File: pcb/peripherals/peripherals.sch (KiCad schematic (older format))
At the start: 10 parts, among them J101 Conn_01x04, J102 Conn_01x04, J103 Conn_01x04, J104 Conn_01x04, J105 Conn_01x04, J106 Conn_01x04, J107 Conn_01x04, J108 Conn_01x04

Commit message: Layout finished and Gerbers generated
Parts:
- removed J101, J102, J107, J108: Conn_01x04, Socket_Strips:Socket_Strip_Straight_1x04_Pitch2.54mm, symbol Connector_Generic:Conn_01x04
- added J101, J102, J107, J108: Conn_01x05, Socket_Strips:Socket_Strip_Straight_1x05_Pitch2.54mm, symbol Connector_Generic:Conn_01x05
- added MH101, MH102, MH103, MH104: MountingHole, Mounting_Holes:MountingHole_5.3mm_M5_Pad, symbol Mechanical:MountingHole
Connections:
- net GND: now also J101.1 (Pin_1), J102.1 (Pin_1), J107.1 (Pin_1), J108.1 (Pin_1)
- net Sheet5B7230C3/EN: now also J107.5 (Pin_5)
- net Sheet5B7230C3/IN: now also J101.5 (Pin_5)
- net sheet5B6E69B5/EN: now also J107.4 (Pin_4)
- net sheet5B6E69B5/IN: now also J101.4 (Pin_4)
- net sheet5B6E69C3/EN: now also J107.3 (Pin_3)
- net sheet5B6E69C3/IN: now also J101.3 (Pin_3)
- net sheet5B6E69C4/EN: now also J107.2 (Pin_2)
- net sheet5B6E69C4/IN: now also J101.2 (Pin_2)
- net sheet5B6E6A5A/EN: now also J108.5 (Pin_5)
- net sheet5B6E6A5A/IN: now also J102.5 (Pin_5)
- net sheet5B6E6A5B/EN: now also J108.4 (Pin_4)
- net sheet5B6E6A5B/IN: now also J102.4 (Pin_4)
- net sheet5B6E6A5C/EN: now also J108.3 (Pin_3)
- net sheet5B6E6A5C/IN: now also J102.3 (Pin_3)
- net sheet5B6E6A5D/EN: now also J108.2 (Pin_2)
- net sheet5B6E6A5D/IN: now also J102.2 (Pin_2)
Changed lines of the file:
@@
 Wire Wire Line
 	950  2850 1100 2850
-$Comp
-L Connector_Generic:Conn_01x04 J101
-U 1 1 5B6FBC4E
+Wire Wire Line
+	3400 3950 3900 3950
+Wire Wire Line
+	3900 3950 3900 4250
+Wire Wire Line
+	3900 4250 4050 4250
+Wire Wire Line
+	3400 3850 3900 3850
+Wire Wire Line
+	3900 3850 3900 3550
+Wire Wire Line
+	3900 3550 4050 3550
+Wire Wire Line
+	3400 3750 3850 3750
+Wire Wire Line
+	3850 3750 3850 2800
+Wire Wire Line
+	3850 2800 4050 2800
+Wire Wire Line
+	3400 3650 3800 3650
+Wire Wire Line
+	3800 3650 3800 2100
+Wire Wire Line
+	3800 2100 4050 2100
+Wire Wire Line
+	3400 2300 3600 2300
+Wire Wire Line
+	3600 2300 3600 2600
+Wire Wire Line
+	3600 2600 4050 2600
+Wire Wire Line
+	3400 2400 3550 2400
+Wire Wire Line
+	3550 2400 3550 3350
+Wire Wire Line
+	3550 3350 4050 3350
+Wire Wire Line
+	3400 2500 3500 2500
+Wire Wire Line
+	3500 2500 3500 4050
+Wire Wire Line
+	3500 4050 4050 4050
+Wire Wire Line
+	3400 2200 3600 2200
+Wire Wire Line
+	3600 2200 3600 1900
+Wire Wire Line
+	3600 1900 4050 1900
+Wire Wire Line
+	6750 3950 7250 3950
+Wire Wire Line
+	7250 3950 7250 4250
+Wire Wire Line
+	7250 4250 7400 4250
+Wire Wire Line
+	6750 3850 7250 3850
+Wire Wire Line
+	7250 3850 7250 3550
+Wire Wire Line
+	7250 3550 7400 3550
+Wire Wire Line
+	6750 3750 7200 3750
+Wire Wire Line
+	7200 3750 7200 2800
+Wire Wire Line
+	7200 2800 7400 2800
+Wire Wire Line
+	6750 3650 7150 3650
+Wire Wire Line
+	7150 3650 7150 2100
+Wire Wire Line
+	7150 2100 7400 2100
+Wire Wire Line
+	6750 2300 6950 2300
+Wire Wire Line
+	6950 2300 6950 2600
+Wire Wire Line
+	6950 2600 7400 2600
+Wire Wire Line
+	6750 2400 6900 2400
+Wire Wire Line
+	6900 2400 6900 3350
+Wire Wire Line
+	6900 3350 7400 3350
+Wire Wire Line
+	6750 2500 6850 2500
+Wire Wire Line
+	6850 2500 6850 4050
+Wire Wire Line
+	6850 4050 7400 4050
+Wire Wire Line
+	6750 2200 6950 2200
+Wire Wire Line
+	6950 2200 6950 1900
+Wire Wire Line
+	6950 1900 7400 1900
+$Comp
+L Connector_Generic:Conn_01x05 J101
+U 1 1 5B71A22D
 P 3200 2400
 F 0 "J101" H 3120 1975 50  0000 C CNN
-F 1 "Conn_01x04" H 3120 2066 50  0000 C CNN
-F 2 "Socket_Strips:Socket_Strip_Straight_1x04_Pitch2.54mm" H 3200 2400 50  0001 C CNN
+F 1 "Conn_01x05" H 3120 2066 50  0000 C CNN
+F 2 "Socket_Strips:Socket_Strip_Straight_1x05_Pitch2.54mm" H 3200 2400 50  0001 C CNN
 F 3 "~" H 3200 2400 50  0001 C CNN
 F 4 "NoPart" H 3200 2400 50  0001 C CNN "Mouser"
@@
 $EndComp
 $Comp
-L Connector_Generic:Conn_01x04 J107
-U 1 1 5B6FBCEC
+L power:GND #PWR0105
+U 1 1 5B71A5D7
+P 3450 2700
+F 0 "#PWR0105" H 3450 2450 50  0001 C CNN
+F 1 "GND" H 3455 2527 50  0000 C CNN
+F 2 "" H 3450 2700 50  0001 C CNN
+F 3 "" H 3450 2700 50  0001 C CNN
+	1    3450 2700
+	1    0    0    -1
+$EndComp
+Wire Wire Line
+	3450 2700 3450 2600
+Wire Wire Line
+	3450 2600 3400 2600
+$Comp
+L Connector_Generic:Conn_01x05 J107
+U 1 1 5B71D263
 P 3200 3850
 F 0 "J107" H 3120 3425 50  0000 C CNN
-F 1 "Conn_01x04" H 3120 3516 50  0000 C CNN
-F 2 "Socket_Strips:Socket_Strip_Straight_1x04_Pitch2.54mm" H 3200 3850 50  0001 C CNN
+F 1 "Conn_01x05" H 3120 3516 50  0000 C CNN
+F 2 "Socket_Strips:Socket_Strip_Straight_1x05_Pitch2.54mm" H 3200 3850 50  0001 C CNN
 F 3 "~" H 3200 3850 50  0001 C CNN
 F 4 "NoPart" H 3200 3850 50  0001 C CNN "Mouser"
@@
 	-1   0    0    1
 $EndComp
-Wire Wire Line
-	3400 3950 3900 3950
-Wire Wire Line
-	3900 3950 3900 4250
-Wire Wire Line
-	3900 4250 4050 4250
-Wire Wire Line
-	3400 3850 3900 3850
-Wire Wire Line
-	3900 3850 3900 3550
-Wire Wire Line
-	3900 3550 4050 3550
-Wire Wire Line
-	3400 3750 3850 3750
-Wire Wire Line
-	3850 3750 3850 2800
-Wire Wire Line
-	3850 2800 4050 2800
-Wire Wire Line
-	3400 3650 3800 3650
-Wire Wire Line
-	3800 3650 3800 2100
-Wire Wire Line
-	3800 2100 4050 2100
-Wire Wire Line
-	3400 2300 3600 2300
-Wire Wire Line
-	3600 2300 3600 2600
-Wire Wire Line
-	3600 2600 4050 2600
-Wire Wire Line
-	3400 2400 3550 2400
-Wire Wire Line
-	3550 2400 3550 3350
-Wire Wire Line
-	3550 3350 4050 3350
-Wire Wire Line
-	3400 2500 3500 2500
-Wire Wire Line
-	3500 2500 3500 4050
-Wire Wire Line
-	3500 4050 4050 4050
-Wire Wire Line
-	3400 2200 3600 2200
-Wire Wire Line
-	3600 2200 3600 1900
-Wire Wire Line
-	3600 1900 4050 1900
-$Comp
-L Connector_Generic:Conn_01x04 J102
-U 1 1 5B70643C
+$Comp
+L Connector_Generic:Conn_01x05 J102
+U 1 1 5B71D2AF
 P 6550 2400
 F 0 "J102" H 6470 1975 50  0000 C CNN
-F 1 "Conn_01x04" H 6470 2066 50  0000 C CNN
-F 2 "Socket_Strips:Socket_Strip_Straight_1x04_Pitch2.54mm" H 6550 2400 50  0001 C CNN
+F 1 "Conn_01x05" H 6470 2066 50  0000 C CNN
+F 2 "Socket_Strips:Socket_Strip_Straight_1x05_Pitch2.54mm" H 6550 2400 50  0001 C CNN
 F 3 "~" H 6550 2400 50  0001 C CNN
 F 4 "NoPart" H 6550 2400 50  0001 C CNN "Mouser"
@@
 $EndComp
 $Comp
-L Connector_Generic:Conn_01x04 J108
-U 1 1 5B706443
+L Connector_Generic:Conn_01x05 J108
+U 1 1 5B71D307
 P 6550 3850
 F 0 "J108" H 6470 3425 50  0000 C CNN
-F 1 "Conn_01x04" H 6470 3516 50  0000 C CNN
-F 2 "Socket_Strips:Socket_Strip_Straight_1x04_Pitch2.54mm" H 6550 3850 50  0001 C CNN
+F 1 "Conn_01x05" H 6470 3516 50  0000 C CNN
+F 2 "Socket_Strips:Socket_Strip_Straight_1x05_Pitch2.54mm" H 6550 3850 50  0001 C CNN
 F 3 "~" H 6550 3850 50  0001 C CNN
 F 4 "NoPart" H 6550 3850 50  0001 C CNN "Mouser"
@@
 	-1   0    0    1
 $EndComp
-Wire Wire Line
-	6750 3950 7250 3950
-Wire Wire Line
-	7250 3950 7250 4250
-Wire Wire Line
-	7250 4250 7400 4250
-Wire Wire Line
-	6750 3850 7250 3850
-Wire Wire Line
-	7250 3850 7250 3550
-Wire Wire Line
-	7250 3550 7400 3550
-Wire Wire Line
-	6750 3750 7200 3750
-Wire Wire Line
-	7200 3750 7200 2800
-Wire Wire Line
-	7200 2800 7400 2800
-Wire Wire Line
-	6750 3650 7150 3650
-Wire Wire Line
-	7150 3650 7150 2100
-Wire Wire Line
-	7150 2100 7400 2100
-Wire Wire Line
-	6750 2300 6950 2300
-Wire Wire Line
-	6950 2300 6950 2600
-Wire Wire Line
-	6950 2600 7400 2600
-Wire Wire Line
-	6750 2400 6900 2400
-Wire Wire Line
-	6900 2400 6900 3350
-Wire Wire Line
-	6900 3350 7400 3350
-Wire Wire Line
-	6750 2500 6850 2500
-Wire Wire Line
-	6850 2500 6850 4050
-Wire Wire Line
-	6850 4050 7400 4050
-Wire Wire Line
-	6750 2200 6950 2200
-Wire Wire Line
-	6950 2200 6950 1900
-Wire Wire Line
-	6950 1900 7400 1900
+$Comp
+L power:GND #PWR0107
+U 1 1 5B71D394
+P 3450 4200
+F 0 "#PWR0107" H 3450 3950 50  0001 C CNN
+F 1 "GND" H 3455 4027 50  0000 C CNN
+F 2 "" H 3450 4200 50  0001 C CNN
+F 3 "" H 3450 4200 50  0001 C CNN
+	1    3450 4200
+	1    0    0    -1
+$EndComp
+Wire Wire Line
+	3450 4200 3450 4050
+Wire Wire Line
+	3450 4050 3400 4050
+$Comp
+L power:GND #PWR0108
+U 1 1 5B720152
+P 6800 4200
+F 0 "#PWR0108" H 6800 3950 50  0001 C CNN
+F 1 "GND" H 6805 4027 50  0000 C CNN
+F 2 "" H 6800 4200 50  0001 C CNN
+F 3 "" H 6800 4200 50  0001 C CNN
+	1    6800 4200
+	1    0    0    -1
+$EndComp
+Wire Wire Line
+	6800 4200 6800 4050
+Wire Wire Line
+	6800 4050 6750 4050
+$Comp
+L power:GND #PWR0106
+U 1 1 5B723175
+P 6800 2750
+F 0 "#PWR0106" H 6800 2500 50  0001 C CNN
+F 1 "GND" H 6805 2577 50  0000 C CNN
+F 2 "" H 6800 2750 50  0001 C CNN
+F 3 "" H 6800 2750 50  0001 C CNN
+	1    6800 2750
+	1    0    0    -1
+$EndComp
+Wire Wire Line
+	6800 2750 6800 2600
+Wire Wire Line
+	6800 2600 6750 2600
+$Comp
+L Mechanical:MountingHole MH101
+U 1 1 5B72BC06
+P 2300 6000
+F 0 "MH101" H 2400 6046 50  0000 L CNN
+F 1 "MountingHole" H 2400 5955 50  0000 L CNN
+F 2 "Mounting_Holes:MountingHole_5.3mm_M5_Pad" H 2300 6000 50  0001 C CNN
+F 3 "~" H 2300 6000 50  0001 C CNN
+F 4 "NoPart" H 2300 6000 50  0001 C CNN "Mouser"
+	1    2300 6000
+	1    0    0    -1
+$EndComp
+$Comp
+L Mechanical:MountingHole MH102
+U 1 1 5B731ED4
+P 2300 6250
+F 0 "MH102" H 2400 6296 50  0000 L CNN
+F 1 "MountingHole" H 2400 6205 50  0000 L CNN
+F 2 "Mounting_Holes:MountingHole_5.3mm_M5_Pad" H 2300 6250 50  0001 C CNN
+F 3 "~" H 2300 6250 50  0001 C CNN
+F 4 "NoPart" H 2300 6250 50  0001 C CNN "Mouser"
+	1    2300 6250
+	1    0    0    -1
+$EndComp
+$Comp
+L Mechanical:MountingHole MH103
+U 1 1 5B734FC8
+P 2300 6550
+F 0 "MH103" H 2400 6596 50  0000 L CNN
+F 1 "MountingHole" H 2400 6505 50  0000 L CNN
+F 2 "Mounting_Holes:MountingHole_5.3mm_M5_Pad" H 2300 6550 50  0001 C CNN
+F 3 "~" H 2300 6550 50  0001 C CNN
+F 4 "NoPart" H 2300 6550 50  0001 C CNN "Mouser"
+	1    2300 6550
+	1    0    0    -1
+$EndComp
+$Comp
+L Mechanical:MountingHole MH104
+U 1 1 5B734FCF
+P 2300 6800
+F 0 "MH104" H 2400 6846 50  0000 L CNN
+F 1 "MountingHole" H 2400 6755 50  0000 L CNN
+F 2 "Mounting_Holes:MountingHole_5.3mm_M5_Pad" H 2300 6800 50  0001 C CNN
+F 3 "~" H 2300 6800 50  0001 C CNN
+F 4 "NoPart" H 2300 6800 50  0001 C CNN "Mouser"
+	1    2300 6800
+	1    0    0    -1
+$EndComp
 $EndSCHEMATC

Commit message: Save before autotile
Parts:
- added C101, C102: 470uF, Capacitors_ThroughHole:CP_Radial_D10.0mm_P5.00mm, symbol Device:C_Small
- added C103, C104: 1000uF, Capacitors_ThroughHole:CP_Radial_D18.0mm_P7.50mm, symbol Device:C_Small
- J103, J104, J105, J106: footprint peripherals:Conn-4-8mmx6mm -> peripherals:Conn-4-8mmx3mm
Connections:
- net +BATT: now also C101.1, C102.1, C103.1, C104.1
- net GND: now also C101.2, C102.2, C103.2, C104.2
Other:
- moved on the sheet: J101, J102, J103, J104, J105, J106, J107, J108

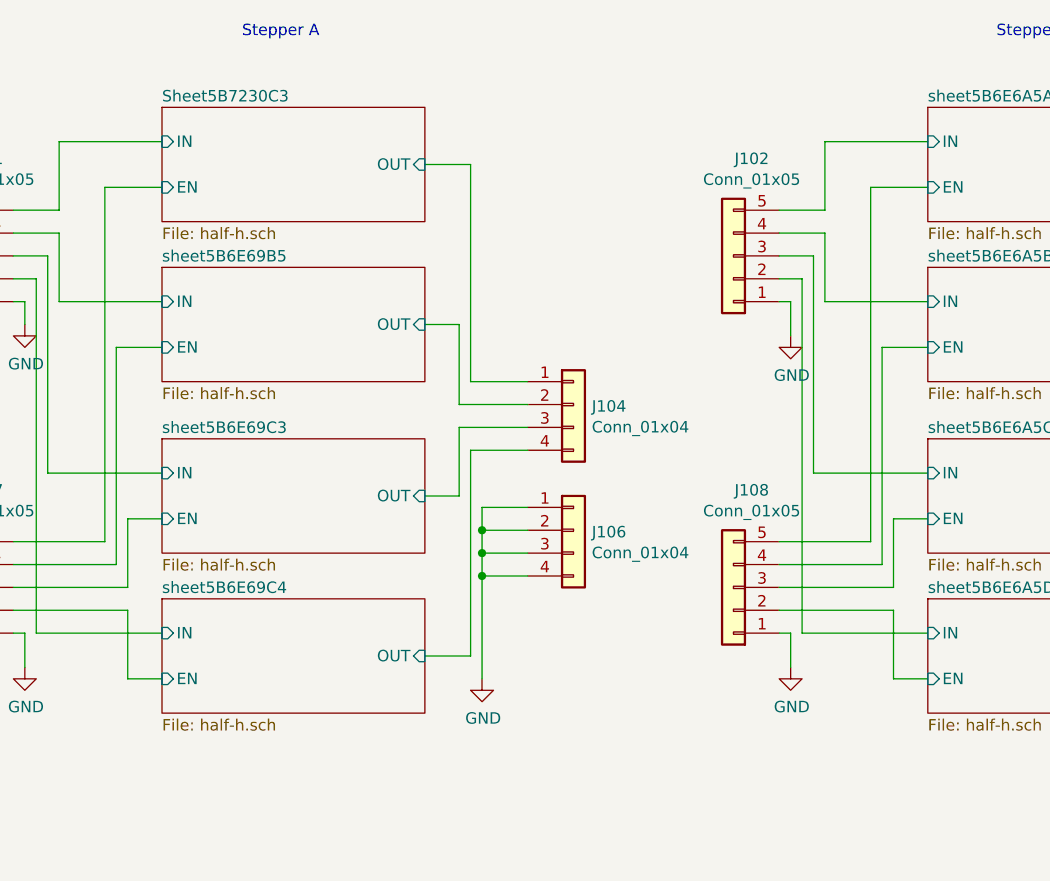
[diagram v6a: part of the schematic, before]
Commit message: Redesign peripheral PCB, simulate photodiode circuit
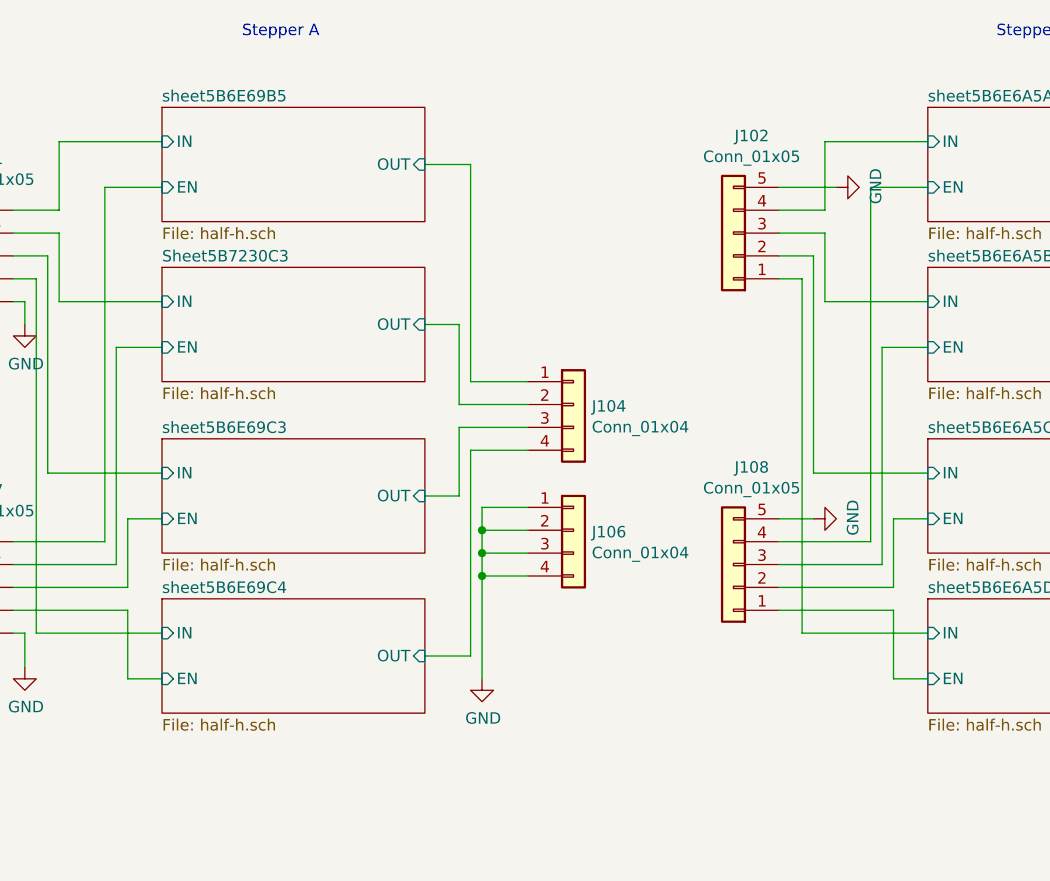
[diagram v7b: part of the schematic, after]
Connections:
- net GND: now also J102.5 (Pin_5), J108.5 (Pin_5); no longer J102.1 (Pin_1), J108.1 (Pin_1)
- net Sheet5B7230C3/EN: now also J107.4 (Pin_4); no longer J107.5 (Pin_5)
- net Sheet5B7230C3/IN: now also J101.4 (Pin_4); no longer J101.5 (Pin_5)
- net Sheet5B7230C3/OUT: now also J104.2 (Pin_2); no longer J104.1 (Pin_1)
- net sheet5B6E69B5/EN: now also J107.5 (Pin_5); no longer J107.4 (Pin_4)
- net sheet5B6E69B5/IN: now also J101.5 (Pin_5); no longer J101.4 (Pin_4)
- net sheet5B6E69B5/OUT: now also J104.1 (Pin_1); no longer J104.2 (Pin_2)
- net sheet5B6E6A5A/EN: now also J108.4 (Pin_4); no longer J108.5 (Pin_5)
- net sheet5B6E6A5A/IN: now also J102.4 (Pin_4); no longer J102.5 (Pin_5)
- net sheet5B6E6A5B/EN: now also J108.3 (Pin_3); no longer J108.4 (Pin_4)
- net sheet5B6E6A5B/IN: now also J102.3 (Pin_3); no longer J102.4 (Pin_4)
- net sheet5B6E6A5C/EN: now also J108.2 (Pin_2); no longer J108.3 (Pin_3)
- net sheet5B6E6A5C/IN: now also J102.2 (Pin_2); no longer J102.3 (Pin_3)
- net sheet5B6E6A5D/EN: now also J108.1 (Pin_1); no longer J108.2 (Pin_2)
- net sheet5B6E6A5D/IN: now also J102.1 (Pin_1); no longer J102.2 (Pin_2)
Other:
- moved on the sheet: J102, J108
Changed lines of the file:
@@
 $EndDescr
 $Sheet
-S 4850 1750 1150 500
+S 4850 2450 1150 500
 U 5B7230C4
 F0 "Sheet5B7230C3" 50
+F1 "half-h.sch" 50
+F2 "OUT" I R 6000 2700 50
+F3 "IN" I L 4850 2600 50
+F4 "EN" I L 4850 2800 50
+$EndSheet
+$Sheet
+S 4850 1750 1150 500
+U 5B6E69BA
+F0 "sheet5B6E69B5" 50
 F1 "half-h.sch" 50
 F2 "OUT" I R 6000 2000 50
 F3 "IN" I L 4850 1900 50
 F4 "EN" I L 4850 2100 50
-$EndSheet
-$Sheet
-S 4850 2450 1150 500
-U 5B6E69BA
-F0 "sheet5B6E69B5" 50
-F1 "half-h.sch" 50
-F2 "OUT" I R 6000 2700 50
-F3 "IN" I L 4850 2600 50
-F4 "EN" I L 4850 2800 50
 $EndSheet
 $Sheet
@@
 	7700 2400 7700 3350
 Wire Wire Line
-	7700 3350 8200 3350
-Wire Wire Line
 	7550 2500 7650 2500
 Wire Wire Line
@@
 L Connector_Generic:Conn_01x05 J102
 U 1 1 5B71D2AF
-P 7350 2400
-F 0 "J102" H 7270 1975 50  0000 C CNN
-F 1 "Conn_01x05" H 7270 2066 50  0000 C CNN
-F 2 "Socket_Strips:Socket_Strip_Straight_1x05_Pitch2.54mm" H 7350 2400 50  0001 C CNN
-F 3 "~" H 7350 2400 50  0001 C CNN
-F 4 "NoPart" H 7350 2400 50  0001 C CNN "Mouser"
-	1    7350 2400
+P 7350 2300
+F 0 "J102" H 7270 1875 50  0000 C CNN
+F 1 "Conn_01x05" H 7270 1966 50  0000 C CNN
+F 2 "Socket_Strips:Socket_Strip_Straight_1x05_Pitch2.54mm" H 7350 2300 50  0001 C CNN
+F 3 "~" H 7350 2300 50  0001 C CNN
+F 4 "NoPart" H 7350 2300 50  0001 C CNN "Mouser"
+	1    7350 2300
 	-1   0    0    1
 $EndComp
@@
 L Connector_Generic:Conn_01x05 J108
 U 1 1 5B71D307
-P 7350 3850
-F 0 "J108" H 7270 3425 50  0000 C CNN
-F 1 "Conn_01x05" H 7270 3516 50  0000 C CNN
-F 2 "Socket_Strips:Socket_Strip_Straight_1x05_Pitch2.54mm" H 7350 3850 50  0001 C CNN
-F 3 "~" H 7350 3850 50  0001 C CNN
-F 4 "NoPart" H 7350 3850 50  0001 C CNN "Mouser"
-	1    7350 3850
+P 7350 3750
+F 0 "J108" H 7270 3325 50  0000 C CNN
+F 1 "Conn_01x05" H 7270 3416 50  0000 C CNN
+F 2 "Socket_Strips:Socket_Strip_Straight_1x05_Pitch2.54mm" H 7350 3750 50  0001 C CNN
+F 3 "~" H 7350 3750 50  0001 C CNN
+F 4 "NoPart" H 7350 3750 50  0001 C CNN "Mouser"
+	1    7350 3750
 	-1   0    0    1
 $EndComp
@@
 L power:GND #PWR0108
 U 1 1 5B720152
-P 7600 4200
-F 0 "#PWR0108" H 7600 3950 50  0001 C CNN
-F 1 "GND" H 7605 4027 50  0000 C CNN
-F 2 "" H 7600 4200 50  0001 C CNN
-F 3 "" H 7600 4200 50  0001 C CNN
-	1    7600 4200
-	1    0    0    -1
-$EndComp
-Wire Wire Line
-	7600 4200 7600 4050
-Wire Wire Line
-	7600 4050 7550 4050
+P 7700 3550
+F 0 "#PWR0108" H 7700 3300 50  0001 C CNN
+F 1 "GND" H 7705 3377 50  0000 C CNN
+F 2 "" H 7700 3550 50  0001 C CNN
+F 3 "" H 7700 3550 50  0001 C CNN
+	1    7700 3550
+	0    -1   -1   0
+$EndComp
 $Comp
 L power:GND #PWR0106
 U 1 1 5B723175
-P 7600 2750
-F 0 "#PWR0106" H 7600 2500 50  0001 C CNN
-F 1 "GND" H 7605 2577 50  0000 C CNN
-F 2 "" H 7600 2750 50  0001 C CNN
-F 3 "" H 7600 2750 50  0001 C CNN
-	1    7600 2750
-	1    0    0    -1
-$EndComp
-Wire Wire Line
-	7600 2750 7600 2600
-Wire Wire Line
-	7600 2600 7550 2600
+P 7800 2100
+F 0 "#PWR0106" H 7800 1850 50  0001 C CNN
+F 1 "GND" H 7805 1927 50  0000 C CNN
+F 2 "" H 7800 2100 50  0001 C CNN
+F 3 "" H 7800 2100 50  0001 C CNN
+	1    7800 2100
+	0    -1   -1   0
+$EndComp
 $Comp
 L Mechanical:MountingHole MH101
@@
 Connection ~ 2050 2300
 Connection ~ 1600 2300
+Wire Wire Line
+	7700 3350 8200 3350
+Wire Wire Line
+	7700 3550 7550 3550
+Wire Wire Line
+	7800 2100 7550 2100
 $EndSCHEMATC
